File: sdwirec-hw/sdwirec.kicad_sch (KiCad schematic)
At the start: 66 parts, among them IC1 USB2640-HZH-02, IC2 MC74HC1G04DTT1G, J1 USB_C_Receptacle_USB2.0, J2 usd_plug, J3 Micro_SD_Card, Q1 SMMBT4403L, Q2 SMMBT4403L, U1 M24C02-RDW, U2 SPX3819M5-L-3-3, U3 TS3A27518EPW, U4 FT200XD, Y1 24Mhz

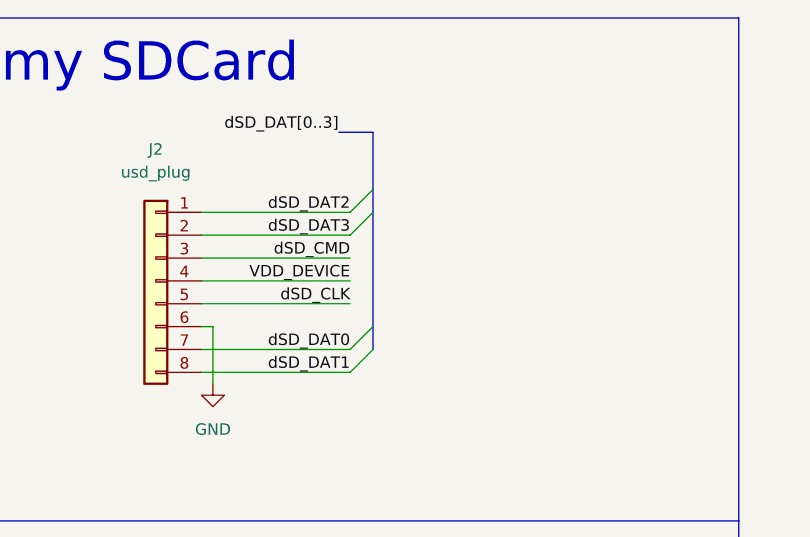
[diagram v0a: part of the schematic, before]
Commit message: add schottky diode to vdd_device line
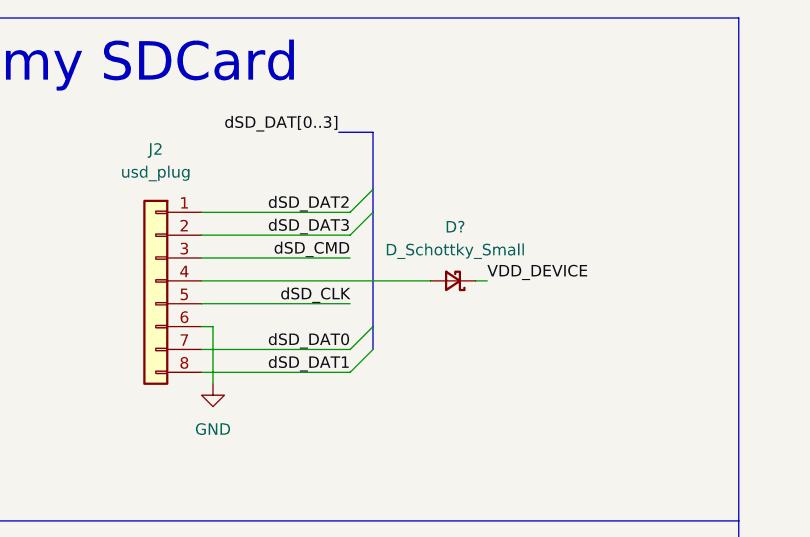
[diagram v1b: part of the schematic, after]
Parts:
- added D?: D_Schottky_Small, symbol Device:D_Schottky_Small
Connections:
- net VDD_DEVICE: now also D?.1 (K); no longer J2.4 (Pin_4)
- new net: D?.2 (A), J2.4 (Pin_4)
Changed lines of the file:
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@@
     (title "Badgerd - SDWireC")
     (date "2023-03-02")
-    (rev "1.2")
+    (rev "1.3")
     (company "Badgerd Technologies B.V.")
     (comment 1 "Talha Can Havadar")
@@
     (stroke (width 0) (type default) (color 0 0 0 0))
   )
-  (wire (pts (xy 251.46 41.91) (xy 267.97 41.91))
-    (stroke (width 0) (type default) (color 0 0 0 0))
-  )
   (wire (pts (xy 351.155 55.88) (xy 356.87 55.88))
     (stroke (width 0) (type default) (color 0 0 0 0))
@@
     (stroke (width 0) (type default) (color 0 0 0 0))
   )
+  (wire (pts (xy 251.46 41.91) (xy 276.86 41.91))
+    (stroke (width 0) (type default) (color 0 0 0 0))
+  )
   (wire (pts (xy 104.14 106.68) (xy 115.062 106.68))
     (stroke (width 0) (type default) (color 0 0 0 0))
@@
     (stroke (width 0) (type default) (color 0 0 0 0))
   )
+  (wire (pts (xy 281.94 41.91) (xy 283.21 41.91))
+    (stroke (width 0) (type default) (color 0 0 0 0))
+  )
   (wire (pts (xy 48.26 214.63) (xy 48.26 227.33))
     (stroke (width 0) (type default) (color 0 0 0 0))
@@
     (effects (font (size 1.27 1.27)) (justify right bottom))
   )
-  (label "VDD_DEVICE" (at 267.97 41.91 180)
-    (effects (font (size 1.27 1.27)) (justify right bottom))
+  (label "VDD_DEVICE" (at 283.21 41.91 0)
+    (effects (font (size 1.27 1.27)) (justify left bottom))
   )
   (label "SD_CLK" (at 193.675 217.805 0)
@@
     (pin "1")
   )
+  (symbol (lib_id "Device:D_Schottky_Small") (at 279.4 41.91 180) (unit 1)
+    (in_bom yes) (on_board yes) (fields_autoplaced)
+    (property "Reference" "D?" (id 0) (at 279.654 35.941 0))
+    (property "Value" "D_Schottky_Small" (id 1) (at 279.654 38.481 0))
+    (property "Footprint" "" (id 2) (at 279.4 41.91 90)
+      (effects (font (size 1.27 1.27)) hide)
+    )
+    (property "Datasheet" "~" (id 3) (at 279.4 41.91 90)
+      (effects (font (size 1.27 1.27)) hide)
+    )
+    (pin "1")
+    (pin "2")
+  )
   (symbol (lib_id "power:+3V3") (at 147.32 200.66 270) (unit 1)
     (in_bom yes) (on_board yes)
@@
       (reference "D4") (unit 1) (value "Yellow") (footprint "LED_SMD:LED_0402_1005Metric")
     )
+    (path "/131c4874-ecd5-442f-a7ee-a8fa39e5cc1d"
+      (reference "D?") (unit 1) (value "D_Schottky_Small") (footprint "")
+    )
     (path "/f27184be-59d2-4453-986f-21a7476ed0b7"
